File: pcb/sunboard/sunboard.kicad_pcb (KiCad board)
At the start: 2 copper layers, 3 parts, among them U1 CD74HC4067M, U2 CD74HC4067M, U3 ESP32_NODEMCU

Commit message: feat(pcb): remove led driver, layout main grid
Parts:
- added D1: WS2812B, LED_SMD:LED_WS2812B_PLCC4_5.0x5.0mm_P3.2mm, F.Cu at (20.0, 17.5)
- added D10: WS2812B, LED_SMD:LED_WS2812B_PLCC4_5.0x5.0mm_P3.2mm, F.Cu at (110.0, 17.5)
- added D100: WS2812B, LED_SMD:LED_WS2812B_PLCC4_5.0x5.0mm_P3.2mm, F.Cu at (20.0, 152.5)
- added D101: WS2812B, LED_SMD:LED_WS2812B_PLCC4_5.0x5.0mm_P3.2mm, F.Cu at (30.0, 152.5)
- added D102: WS2812B, LED_SMD:LED_WS2812B_PLCC4_5.0x5.0mm_P3.2mm, F.Cu at (40.0, 152.5)
- added D103: WS2812B, LED_SMD:LED_WS2812B_PLCC4_5.0x5.0mm_P3.2mm, F.Cu at (50.0, 152.5)
- added D104: WS2812B, LED_SMD:LED_WS2812B_PLCC4_5.0x5.0mm_P3.2mm, F.Cu at (60.0, 152.5)
- added D105: WS2812B, LED_SMD:LED_WS2812B_PLCC4_5.0x5.0mm_P3.2mm, F.Cu at (70.0, 152.5)
- added D106: WS2812B, LED_SMD:LED_WS2812B_PLCC4_5.0x5.0mm_P3.2mm, F.Cu at (80.0, 152.5)
- added D107: WS2812B, LED_SMD:LED_WS2812B_PLCC4_5.0x5.0mm_P3.2mm, F.Cu at (90.0, 152.5)
- added D108: WS2812B, LED_SMD:LED_WS2812B_PLCC4_5.0x5.0mm_P3.2mm, F.Cu at (100.0, 152.5)
- added D109: WS2812B, LED_SMD:LED_WS2812B_PLCC4_5.0x5.0mm_P3.2mm, F.Cu at (110.0, 152.5)
- added D11: WS2812B, LED_SMD:LED_WS2812B_PLCC4_5.0x5.0mm_P3.2mm, F.Cu at (120.0, 17.5)
- added D110: WS2812B, LED_SMD:LED_WS2812B_PLCC4_5.0x5.0mm_P3.2mm, F.Cu at (120.0, 152.5)
- added D111: WS2812B, LED_SMD:LED_WS2812B_PLCC4_5.0x5.0mm_P3.2mm, F.Cu at (20.0, 167.5)
- added D112: WS2812B, LED_SMD:LED_WS2812B_PLCC4_5.0x5.0mm_P3.2mm, F.Cu at (30.0, 167.5)
- added D113: WS2812B, LED_SMD:LED_WS2812B_PLCC4_5.0x5.0mm_P3.2mm, F.Cu at (40.0, 167.5)
- added D114: WS2812B, LED_SMD:LED_WS2812B_PLCC4_5.0x5.0mm_P3.2mm, F.Cu at (50.0, 167.5)
- added D115: WS2812B, LED_SMD:LED_WS2812B_PLCC4_5.0x5.0mm_P3.2mm, F.Cu at (60.0, 167.5)
- added D116: WS2812B, LED_SMD:LED_WS2812B_PLCC4_5.0x5.0mm_P3.2mm, F.Cu at (70.0, 167.5)
- added D117: WS2812B, LED_SMD:LED_WS2812B_PLCC4_5.0x5.0mm_P3.2mm, F.Cu at (80.0, 167.5)
- added D118: WS2812B, LED_SMD:LED_WS2812B_PLCC4_5.0x5.0mm_P3.2mm, F.Cu at (90.0, 167.5)
- added D119: WS2812B, LED_SMD:LED_WS2812B_PLCC4_5.0x5.0mm_P3.2mm, F.Cu at (100.0, 167.5)
- added D12: WS2812B, LED_SMD:LED_WS2812B_PLCC4_5.0x5.0mm_P3.2mm, F.Cu at (20.0, 32.5)
- added D120: WS2812B, LED_SMD:LED_WS2812B_PLCC4_5.0x5.0mm_P3.2mm, F.Cu at (110.0, 167.5)
- added D121: WS2812B, LED_SMD:LED_WS2812B_PLCC4_5.0x5.0mm_P3.2mm, F.Cu at (120.0, 167.5)
- added D122: WS2812B, LED_SMD:LED_WS2812B_PLCC4_5.0x5.0mm_P3.2mm, F.Cu at (20.0, 182.5)
- added D123: WS2812B, LED_SMD:LED_WS2812B_PLCC4_5.0x5.0mm_P3.2mm, F.Cu at (30.0, 182.5)
- added D124: WS2812B, LED_SMD:LED_WS2812B_PLCC4_5.0x5.0mm_P3.2mm, F.Cu at (40.0, 182.5)
- added D125: WS2812B, LED_SMD:LED_WS2812B_PLCC4_5.0x5.0mm_P3.2mm, F.Cu at (50.0, 182.5)
- added D126: WS2812B, LED_SMD:LED_WS2812B_PLCC4_5.0x5.0mm_P3.2mm, F.Cu at (60.0, 182.5)
- added D127: WS2812B, LED_SMD:LED_WS2812B_PLCC4_5.0x5.0mm_P3.2mm, F.Cu at (70.0, 182.5)
- added D128: WS2812B, LED_SMD:LED_WS2812B_PLCC4_5.0x5.0mm_P3.2mm, F.Cu at (80.0, 182.5)
- added D129: WS2812B, LED_SMD:LED_WS2812B_PLCC4_5.0x5.0mm_P3.2mm, F.Cu at (90.0, 182.5)
- added D13: WS2812B, LED_SMD:LED_WS2812B_PLCC4_5.0x5.0mm_P3.2mm, F.Cu at (30.0, 32.5)
- added D130: WS2812B, LED_SMD:LED_WS2812B_PLCC4_5.0x5.0mm_P3.2mm, F.Cu at (100.0, 182.5)
- added D131: WS2812B, LED_SMD:LED_WS2812B_PLCC4_5.0x5.0mm_P3.2mm, F.Cu at (110.0, 182.5)
- added D132: WS2812B, LED_SMD:LED_WS2812B_PLCC4_5.0x5.0mm_P3.2mm, F.Cu at (120.0, 182.5)
- added D133: WS2812B, LED_SMD:LED_WS2812B_PLCC4_5.0x5.0mm_P3.2mm, F.Cu at (20.0, 197.5)
- added D134: WS2812B, LED_SMD:LED_WS2812B_PLCC4_5.0x5.0mm_P3.2mm, F.Cu at (30.0, 197.5)
- added D135: WS2812B, LED_SMD:LED_WS2812B_PLCC4_5.0x5.0mm_P3.2mm, F.Cu at (40.0, 197.5)
- added D136: WS2812B, LED_SMD:LED_WS2812B_PLCC4_5.0x5.0mm_P3.2mm, F.Cu at (50.0, 197.5)
- added D137: WS2812B, LED_SMD:LED_WS2812B_PLCC4_5.0x5.0mm_P3.2mm, F.Cu at (60.0, 197.5)
- added D138: WS2812B, LED_SMD:LED_WS2812B_PLCC4_5.0x5.0mm_P3.2mm, F.Cu at (70.0, 197.5)
- added D139: WS2812B, LED_SMD:LED_WS2812B_PLCC4_5.0x5.0mm_P3.2mm, F.Cu at (80.0, 197.5)
- added D14: WS2812B, LED_SMD:LED_WS2812B_PLCC4_5.0x5.0mm_P3.2mm, F.Cu at (40.0, 32.5)
- added D140: WS2812B, LED_SMD:LED_WS2812B_PLCC4_5.0x5.0mm_P3.2mm, F.Cu at (90.0, 197.5)
- added D141: WS2812B, LED_SMD:LED_WS2812B_PLCC4_5.0x5.0mm_P3.2mm, F.Cu at (100.0, 197.5)
- added D142: WS2812B, LED_SMD:LED_WS2812B_PLCC4_5.0x5.0mm_P3.2mm, F.Cu at (110.0, 197.5)
- added D143: WS2812B, LED_SMD:LED_WS2812B_PLCC4_5.0x5.0mm_P3.2mm, F.Cu at (120.0, 197.5)
- added D144: WS2812B, LED_SMD:LED_WS2812B_PLCC4_5.0x5.0mm_P3.2mm, F.Cu at (20.0, 212.5)
- added D145: WS2812B, LED_SMD:LED_WS2812B_PLCC4_5.0x5.0mm_P3.2mm, F.Cu at (30.0, 212.5)
- added D146: WS2812B, LED_SMD:LED_WS2812B_PLCC4_5.0x5.0mm_P3.2mm, F.Cu at (40.0, 212.5)
- added D147: WS2812B, LED_SMD:LED_WS2812B_PLCC4_5.0x5.0mm_P3.2mm, F.Cu at (50.0, 212.5)
- added D148: WS2812B, LED_SMD:LED_WS2812B_PLCC4_5.0x5.0mm_P3.2mm, F.Cu at (60.0, 212.5)
- added D149: WS2812B, LED_SMD:LED_WS2812B_PLCC4_5.0x5.0mm_P3.2mm, F.Cu at (70.0, 212.5)
- added D15: WS2812B, LED_SMD:LED_WS2812B_PLCC4_5.0x5.0mm_P3.2mm, F.Cu at (50.0, 32.5)
- added D150: WS2812B, LED_SMD:LED_WS2812B_PLCC4_5.0x5.0mm_P3.2mm, F.Cu at (80.0, 212.5)
- added D151: WS2812B, LED_SMD:LED_WS2812B_PLCC4_5.0x5.0mm_P3.2mm, F.Cu at (90.0, 212.5)
- added D152: WS2812B, LED_SMD:LED_WS2812B_PLCC4_5.0x5.0mm_P3.2mm, F.Cu at (100.0, 212.5)
- added D153: WS2812B, LED_SMD:LED_WS2812B_PLCC4_5.0x5.0mm_P3.2mm, F.Cu at (110.0, 212.5)
- added D154: WS2812B, LED_SMD:LED_WS2812B_PLCC4_5.0x5.0mm_P3.2mm, F.Cu at (120.0, 212.5)
- added D16: WS2812B, LED_SMD:LED_WS2812B_PLCC4_5.0x5.0mm_P3.2mm, F.Cu at (60.0, 32.5)
- added D17: WS2812B, LED_SMD:LED_WS2812B_PLCC4_5.0x5.0mm_P3.2mm, F.Cu at (70.0, 32.5)
- added D18: WS2812B, LED_SMD:LED_WS2812B_PLCC4_5.0x5.0mm_P3.2mm, F.Cu at (80.0, 32.5)
- added D19: WS2812B, LED_SMD:LED_WS2812B_PLCC4_5.0x5.0mm_P3.2mm, F.Cu at (90.0, 32.5)
- added D2: WS2812B, LED_SMD:LED_WS2812B_PLCC4_5.0x5.0mm_P3.2mm, F.Cu at (30.0, 17.5)
- added D20: WS2812B, LED_SMD:LED_WS2812B_PLCC4_5.0x5.0mm_P3.2mm, F.Cu at (100.0, 32.5)
- added D21: WS2812B, LED_SMD:LED_WS2812B_PLCC4_5.0x5.0mm_P3.2mm, F.Cu at (110.0, 32.5)
- added D22: WS2812B, LED_SMD:LED_WS2812B_PLCC4_5.0x5.0mm_P3.2mm, F.Cu at (120.0, 32.5)
- added D23: WS2812B, LED_SMD:LED_WS2812B_PLCC4_5.0x5.0mm_P3.2mm, F.Cu at (20.0, 47.5)
- added D24: WS2812B, LED_SMD:LED_WS2812B_PLCC4_5.0x5.0mm_P3.2mm, F.Cu at (30.0, 47.5)
- added D25: WS2812B, LED_SMD:LED_WS2812B_PLCC4_5.0x5.0mm_P3.2mm, F.Cu at (40.0, 47.5)
- added D26: WS2812B, LED_SMD:LED_WS2812B_PLCC4_5.0x5.0mm_P3.2mm, F.Cu at (50.0, 47.5)
- added D27: WS2812B, LED_SMD:LED_WS2812B_PLCC4_5.0x5.0mm_P3.2mm, F.Cu at (60.0, 47.5)
- added D28: WS2812B, LED_SMD:LED_WS2812B_PLCC4_5.0x5.0mm_P3.2mm, F.Cu at (70.0, 47.5)
- added D29: WS2812B, LED_SMD:LED_WS2812B_PLCC4_5.0x5.0mm_P3.2mm, F.Cu at (80.0, 47.5)
- added D3: WS2812B, LED_SMD:LED_WS2812B_PLCC4_5.0x5.0mm_P3.2mm, F.Cu at (40.0, 17.5)
- added D30: WS2812B, LED_SMD:LED_WS2812B_PLCC4_5.0x5.0mm_P3.2mm, F.Cu at (90.0, 47.5)
- added D31: WS2812B, LED_SMD:LED_WS2812B_PLCC4_5.0x5.0mm_P3.2mm, F.Cu at (100.0, 47.5)
- added D32: WS2812B, LED_SMD:LED_WS2812B_PLCC4_5.0x5.0mm_P3.2mm, F.Cu at (110.0, 47.5)
- added D33: WS2812B, LED_SMD:LED_WS2812B_PLCC4_5.0x5.0mm_P3.2mm, F.Cu at (120.0, 47.5)
- added D34: WS2812B, LED_SMD:LED_WS2812B_PLCC4_5.0x5.0mm_P3.2mm, F.Cu at (20.0, 62.5)
- added D35: WS2812B, LED_SMD:LED_WS2812B_PLCC4_5.0x5.0mm_P3.2mm, F.Cu at (30.0, 62.5)
- added D36: WS2812B, LED_SMD:LED_WS2812B_PLCC4_5.0x5.0mm_P3.2mm, F.Cu at (40.0, 62.5)
- added D37: WS2812B, LED_SMD:LED_WS2812B_PLCC4_5.0x5.0mm_P3.2mm, F.Cu at (50.0, 62.5)
- added D38: WS2812B, LED_SMD:LED_WS2812B_PLCC4_5.0x5.0mm_P3.2mm, F.Cu at (60.0, 62.5)
- added D39: WS2812B, LED_SMD:LED_WS2812B_PLCC4_5.0x5.0mm_P3.2mm, F.Cu at (70.0, 62.5)
- added D4: WS2812B, LED_SMD:LED_WS2812B_PLCC4_5.0x5.0mm_P3.2mm, F.Cu at (50.0, 17.5)
- added D40: WS2812B, LED_SMD:LED_WS2812B_PLCC4_5.0x5.0mm_P3.2mm, F.Cu at (80.0, 62.5)
- added D41: WS2812B, LED_SMD:LED_WS2812B_PLCC4_5.0x5.0mm_P3.2mm, F.Cu at (90.0, 62.5)
- added D42: WS2812B, LED_SMD:LED_WS2812B_PLCC4_5.0x5.0mm_P3.2mm, F.Cu at (100.0, 62.5)
- added D43: WS2812B, LED_SMD:LED_WS2812B_PLCC4_5.0x5.0mm_P3.2mm, F.Cu at (110.0, 62.5)
- added D44: WS2812B, LED_SMD:LED_WS2812B_PLCC4_5.0x5.0mm_P3.2mm, F.Cu at (120.0, 62.5)
- added D45: WS2812B, LED_SMD:LED_WS2812B_PLCC4_5.0x5.0mm_P3.2mm, F.Cu at (20.0, 77.5)
- added D46: WS2812B, LED_SMD:LED_WS2812B_PLCC4_5.0x5.0mm_P3.2mm, F.Cu at (30.0, 77.5)
- added D47: WS2812B, LED_SMD:LED_WS2812B_PLCC4_5.0x5.0mm_P3.2mm, F.Cu at (40.0, 77.5)
- added D48: WS2812B, LED_SMD:LED_WS2812B_PLCC4_5.0x5.0mm_P3.2mm, F.Cu at (50.0, 77.5)
- added D49: WS2812B, LED_SMD:LED_WS2812B_PLCC4_5.0x5.0mm_P3.2mm, F.Cu at (60.0, 77.5)
- added D5: WS2812B, LED_SMD:LED_WS2812B_PLCC4_5.0x5.0mm_P3.2mm, F.Cu at (60.0, 17.5)
- added D50: WS2812B, LED_SMD:LED_WS2812B_PLCC4_5.0x5.0mm_P3.2mm, F.Cu at (70.0, 77.5)
- added D51: WS2812B, LED_SMD:LED_WS2812B_PLCC4_5.0x5.0mm_P3.2mm, F.Cu at (80.0, 77.5)
- added D52: WS2812B, LED_SMD:LED_WS2812B_PLCC4_5.0x5.0mm_P3.2mm, F.Cu at (90.0, 77.5)
- added D53: WS2812B, LED_SMD:LED_WS2812B_PLCC4_5.0x5.0mm_P3.2mm, F.Cu at (100.0, 77.5)
- added D54: WS2812B, LED_SMD:LED_WS2812B_PLCC4_5.0x5.0mm_P3.2mm, F.Cu at (110.0, 77.5)
- added D55: WS2812B, LED_SMD:LED_WS2812B_PLCC4_5.0x5.0mm_P3.2mm, F.Cu at (120.0, 77.5)
- added D56: WS2812B, LED_SMD:LED_WS2812B_PLCC4_5.0x5.0mm_P3.2mm, F.Cu at (20.0, 92.5)
- added D57: WS2812B, LED_SMD:LED_WS2812B_PLCC4_5.0x5.0mm_P3.2mm, F.Cu at (30.0, 92.5)
- added D58: WS2812B, LED_SMD:LED_WS2812B_PLCC4_5.0x5.0mm_P3.2mm, F.Cu at (40.0, 92.5)
- added D59: WS2812B, LED_SMD:LED_WS2812B_PLCC4_5.0x5.0mm_P3.2mm, F.Cu at (50.0, 92.5)
- added D6: WS2812B, LED_SMD:LED_WS2812B_PLCC4_5.0x5.0mm_P3.2mm, F.Cu at (70.0, 17.5)
- added D60: WS2812B, LED_SMD:LED_WS2812B_PLCC4_5.0x5.0mm_P3.2mm, F.Cu at (60.0, 92.5)
- added D61: WS2812B, LED_SMD:LED_WS2812B_PLCC4_5.0x5.0mm_P3.2mm, F.Cu at (70.0, 92.5)
- added D62: WS2812B, LED_SMD:LED_WS2812B_PLCC4_5.0x5.0mm_P3.2mm, F.Cu at (80.0, 92.5)
- added D63: WS2812B, LED_SMD:LED_WS2812B_PLCC4_5.0x5.0mm_P3.2mm, F.Cu at (90.0, 92.5)
- added D64: WS2812B, LED_SMD:LED_WS2812B_PLCC4_5.0x5.0mm_P3.2mm, F.Cu at (100.0, 92.5)
- added D65: WS2812B, LED_SMD:LED_WS2812B_PLCC4_5.0x5.0mm_P3.2mm, F.Cu at (110.0, 92.5)
- added D66: WS2812B, LED_SMD:LED_WS2812B_PLCC4_5.0x5.0mm_P3.2mm, F.Cu at (120.0, 92.5)
- added D67: WS2812B, LED_SMD:LED_WS2812B_PLCC4_5.0x5.0mm_P3.2mm, F.Cu at (20.0, 107.5)
- added D68: WS2812B, LED_SMD:LED_WS2812B_PLCC4_5.0x5.0mm_P3.2mm, F.Cu at (30.0, 107.5)
- added D69: WS2812B, LED_SMD:LED_WS2812B_PLCC4_5.0x5.0mm_P3.2mm, F.Cu at (40.0, 107.5)
- added D7: WS2812B, LED_SMD:LED_WS2812B_PLCC4_5.0x5.0mm_P3.2mm, F.Cu at (80.0, 17.5)
- added D70: WS2812B, LED_SMD:LED_WS2812B_PLCC4_5.0x5.0mm_P3.2mm, F.Cu at (50.0, 107.5)
- added D71: WS2812B, LED_SMD:LED_WS2812B_PLCC4_5.0x5.0mm_P3.2mm, F.Cu at (60.0, 107.5)
- added D72: WS2812B, LED_SMD:LED_WS2812B_PLCC4_5.0x5.0mm_P3.2mm, F.Cu at (70.0, 107.5)
- added D73: WS2812B, LED_SMD:LED_WS2812B_PLCC4_5.0x5.0mm_P3.2mm, F.Cu at (80.0, 107.5)
- added D74: WS2812B, LED_SMD:LED_WS2812B_PLCC4_5.0x5.0mm_P3.2mm, F.Cu at (90.0, 107.5)
- added D75: WS2812B, LED_SMD:LED_WS2812B_PLCC4_5.0x5.0mm_P3.2mm, F.Cu at (100.0, 107.5)
- added D76: WS2812B, LED_SMD:LED_WS2812B_PLCC4_5.0x5.0mm_P3.2mm, F.Cu at (110.0, 107.5)
- added D77: WS2812B, LED_SMD:LED_WS2812B_PLCC4_5.0x5.0mm_P3.2mm, F.Cu at (120.0, 107.5)
- added D78: WS2812B, LED_SMD:LED_WS2812B_PLCC4_5.0x5.0mm_P3.2mm, F.Cu at (20.0, 122.5)
- added D79: WS2812B, LED_SMD:LED_WS2812B_PLCC4_5.0x5.0mm_P3.2mm, F.Cu at (30.0, 122.5)
- added D8: WS2812B, LED_SMD:LED_WS2812B_PLCC4_5.0x5.0mm_P3.2mm, F.Cu at (90.0, 17.5)
- added D80: WS2812B, LED_SMD:LED_WS2812B_PLCC4_5.0x5.0mm_P3.2mm, F.Cu at (40.0, 122.5)
- added D81: WS2812B, LED_SMD:LED_WS2812B_PLCC4_5.0x5.0mm_P3.2mm, F.Cu at (50.0, 122.5)
- added D82: WS2812B, LED_SMD:LED_WS2812B_PLCC4_5.0x5.0mm_P3.2mm, F.Cu at (60.0, 122.5)
- added D83: WS2812B, LED_SMD:LED_WS2812B_PLCC4_5.0x5.0mm_P3.2mm, F.Cu at (70.0, 122.5)
- added D84: WS2812B, LED_SMD:LED_WS2812B_PLCC4_5.0x5.0mm_P3.2mm, F.Cu at (80.0, 122.5)
- added D85: WS2812B, LED_SMD:LED_WS2812B_PLCC4_5.0x5.0mm_P3.2mm, F.Cu at (90.0, 122.5)
- added D86: WS2812B, LED_SMD:LED_WS2812B_PLCC4_5.0x5.0mm_P3.2mm, F.Cu at (100.0, 122.5)
- added D87: WS2812B, LED_SMD:LED_WS2812B_PLCC4_5.0x5.0mm_P3.2mm, F.Cu at (110.0, 122.5)
- added D88: WS2812B, LED_SMD:LED_WS2812B_PLCC4_5.0x5.0mm_P3.2mm, F.Cu at (120.0, 122.5)
- added D89: WS2812B, LED_SMD:LED_WS2812B_PLCC4_5.0x5.0mm_P3.2mm, F.Cu at (20.0, 137.5)
- added D9: WS2812B, LED_SMD:LED_WS2812B_PLCC4_5.0x5.0mm_P3.2mm, F.Cu at (100.0, 17.5)
- added D90: WS2812B, LED_SMD:LED_WS2812B_PLCC4_5.0x5.0mm_P3.2mm, F.Cu at (30.0, 137.5)
- added D91: WS2812B, LED_SMD:LED_WS2812B_PLCC4_5.0x5.0mm_P3.2mm, F.Cu at (40.0, 137.5)
- added D92: WS2812B, LED_SMD:LED_WS2812B_PLCC4_5.0x5.0mm_P3.2mm, F.Cu at (50.0, 137.5)
- added D93: WS2812B, LED_SMD:LED_WS2812B_PLCC4_5.0x5.0mm_P3.2mm, F.Cu at (60.0, 137.5)
- added D94: WS2812B, LED_SMD:LED_WS2812B_PLCC4_5.0x5.0mm_P3.2mm, F.Cu at (70.0, 137.5)
- added D95: WS2812B, LED_SMD:LED_WS2812B_PLCC4_5.0x5.0mm_P3.2mm, F.Cu at (80.0, 137.5)
- added D96: WS2812B, LED_SMD:LED_WS2812B_PLCC4_5.0x5.0mm_P3.2mm, F.Cu at (90.0, 137.5)
- added D97: WS2812B, LED_SMD:LED_WS2812B_PLCC4_5.0x5.0mm_P3.2mm, F.Cu at (100.0, 137.5)
- added D98: WS2812B, LED_SMD:LED_WS2812B_PLCC4_5.0x5.0mm_P3.2mm, F.Cu at (110.0, 137.5)
- added D99: WS2812B, LED_SMD:LED_WS2812B_PLCC4_5.0x5.0mm_P3.2mm, F.Cu at (120.0, 137.5)
- added SW1: SW_Push, Button_Switch_SMD:SW_Tactile_SPST_NO_Straight_CK_PTS636Sx25SMTRLFS, F.Cu at (20.0, 25.0)
- added SW10: SW_Push, Button_Switch_SMD:SW_Tactile_SPST_NO_Straight_CK_PTS636Sx25SMTRLFS, F.Cu at (110.0, 25.0)
- added SW100: SW_Push, Button_Switch_SMD:SW_Tactile_SPST_NO_Straight_CK_PTS636Sx25SMTRLFS, F.Cu at (20.0, 160.0)
- added SW101: SW_Push, Button_Switch_SMD:SW_Tactile_SPST_NO_Straight_CK_PTS636Sx25SMTRLFS, F.Cu at (30.0, 160.0)
- added SW102: SW_Push, Button_Switch_SMD:SW_Tactile_SPST_NO_Straight_CK_PTS636Sx25SMTRLFS, F.Cu at (40.0, 160.0)
- added SW103: SW_Push, Button_Switch_SMD:SW_Tactile_SPST_NO_Straight_CK_PTS636Sx25SMTRLFS, F.Cu at (50.0, 160.0)
- added SW104: SW_Push, Button_Switch_SMD:SW_Tactile_SPST_NO_Straight_CK_PTS636Sx25SMTRLFS, F.Cu at (60.0, 160.0)
- added SW105: SW_Push, Button_Switch_SMD:SW_Tactile_SPST_NO_Straight_CK_PTS636Sx25SMTRLFS, F.Cu at (70.0, 160.0)
- added SW106: SW_Push, Button_Switch_SMD:SW_Tactile_SPST_NO_Straight_CK_PTS636Sx25SMTRLFS, F.Cu at (80.0, 160.0)
- added SW107: SW_Push, Button_Switch_SMD:SW_Tactile_SPST_NO_Straight_CK_PTS636Sx25SMTRLFS, F.Cu at (90.0, 160.0)
- added SW108: SW_Push, Button_Switch_SMD:SW_Tactile_SPST_NO_Straight_CK_PTS636Sx25SMTRLFS, F.Cu at (100.0, 160.0)
- added SW109: SW_Push, Button_Switch_SMD:SW_Tactile_SPST_NO_Straight_CK_PTS636Sx25SMTRLFS, F.Cu at (110.0, 160.0)
- added SW11: SW_Push, Button_Switch_SMD:SW_Tactile_SPST_NO_Straight_CK_PTS636Sx25SMTRLFS, F.Cu at (120.0, 25.0)
- added SW110: SW_Push, Button_Switch_SMD:SW_Tactile_SPST_NO_Straight_CK_PTS636Sx25SMTRLFS, F.Cu at (120.0, 160.0)
- added SW111: SW_Push, Button_Switch_SMD:SW_Tactile_SPST_NO_Straight_CK_PTS636Sx25SMTRLFS, F.Cu at (20.0, 175.0)
- added SW112: SW_Push, Button_Switch_SMD:SW_Tactile_SPST_NO_Straight_CK_PTS636Sx25SMTRLFS, F.Cu at (30.0, 175.0)
- added SW113: SW_Push, Button_Switch_SMD:SW_Tactile_SPST_NO_Straight_CK_PTS636Sx25SMTRLFS, F.Cu at (40.0, 175.0)
- added SW114: SW_Push, Button_Switch_SMD:SW_Tactile_SPST_NO_Straight_CK_PTS636Sx25SMTRLFS, F.Cu at (50.0, 175.0)
- added SW115: SW_Push, Button_Switch_SMD:SW_Tactile_SPST_NO_Straight_CK_PTS636Sx25SMTRLFS, F.Cu at (60.0, 175.0)
- added SW116: SW_Push, Button_Switch_SMD:SW_Tactile_SPST_NO_Straight_CK_PTS636Sx25SMTRLFS, F.Cu at (70.0, 175.0)
- added SW117: SW_Push, Button_Switch_SMD:SW_Tactile_SPST_NO_Straight_CK_PTS636Sx25SMTRLFS, F.Cu at (80.0, 175.0)
- added SW118: SW_Push, Button_Switch_SMD:SW_Tactile_SPST_NO_Straight_CK_PTS636Sx25SMTRLFS, F.Cu at (90.0, 175.0)
- added SW119: SW_Push, Button_Switch_SMD:SW_Tactile_SPST_NO_Straight_CK_PTS636Sx25SMTRLFS, F.Cu at (100.0, 175.0)
- added SW12: SW_Push, Button_Switch_SMD:SW_Tactile_SPST_NO_Straight_CK_PTS636Sx25SMTRLFS, F.Cu at (20.0, 40.0)
- added SW120: SW_Push, Button_Switch_SMD:SW_Tactile_SPST_NO_Straight_CK_PTS636Sx25SMTRLFS, F.Cu at (110.0, 175.0)
- added SW121: SW_Push, Button_Switch_SMD:SW_Tactile_SPST_NO_Straight_CK_PTS636Sx25SMTRLFS, F.Cu at (120.0, 175.0)
- added SW122: SW_Push, Button_Switch_SMD:SW_Tactile_SPST_NO_Straight_CK_PTS636Sx25SMTRLFS, F.Cu at (20.0, 190.0)
- added SW123: SW_Push, Button_Switch_SMD:SW_Tactile_SPST_NO_Straight_CK_PTS636Sx25SMTRLFS, F.Cu at (30.0, 190.0)
- added SW124: SW_Push, Button_Switch_SMD:SW_Tactile_SPST_NO_Straight_CK_PTS636Sx25SMTRLFS, F.Cu at (40.0, 190.0)
- added SW125: SW_Push, Button_Switch_SMD:SW_Tactile_SPST_NO_Straight_CK_PTS636Sx25SMTRLFS, F.Cu at (50.0, 190.0)
- added SW126: SW_Push, Button_Switch_SMD:SW_Tactile_SPST_NO_Straight_CK_PTS636Sx25SMTRLFS, F.Cu at (60.0, 190.0)
- added SW127: SW_Push, Button_Switch_SMD:SW_Tactile_SPST_NO_Straight_CK_PTS636Sx25SMTRLFS, F.Cu at (70.0, 190.0)
- added SW128: SW_Push, Button_Switch_SMD:SW_Tactile_SPST_NO_Straight_CK_PTS636Sx25SMTRLFS, F.Cu at (80.0, 190.0)
- added SW129: SW_Push, Button_Switch_SMD:SW_Tactile_SPST_NO_Straight_CK_PTS636Sx25SMTRLFS, F.Cu at (90.0, 190.0)
- added SW13: SW_Push, Button_Switch_SMD:SW_Tactile_SPST_NO_Straight_CK_PTS636Sx25SMTRLFS, F.Cu at (30.0, 40.0)
- added SW130: SW_Push, Button_Switch_SMD:SW_Tactile_SPST_NO_Straight_CK_PTS636Sx25SMTRLFS, F.Cu at (100.0, 190.0)
- added SW131: SW_Push, Button_Switch_SMD:SW_Tactile_SPST_NO_Straight_CK_PTS636Sx25SMTRLFS, F.Cu at (110.0, 190.0)
- added SW132: SW_Push, Button_Switch_SMD:SW_Tactile_SPST_NO_Straight_CK_PTS636Sx25SMTRLFS, F.Cu at (120.0, 190.0)
- added SW133: SW_Push, Button_Switch_SMD:SW_Tactile_SPST_NO_Straight_CK_PTS636Sx25SMTRLFS, F.Cu at (20.0, 205.0)
- added SW134: SW_Push, Button_Switch_SMD:SW_Tactile_SPST_NO_Straight_CK_PTS636Sx25SMTRLFS, F.Cu at (30.0, 205.0)
- added SW135: SW_Push, Button_Switch_SMD:SW_Tactile_SPST_NO_Straight_CK_PTS636Sx25SMTRLFS, F.Cu at (40.0, 205.0)
- added SW136: SW_Push, Button_Switch_SMD:SW_Tactile_SPST_NO_Straight_CK_PTS636Sx25SMTRLFS, F.Cu at (50.0, 205.0)
- added SW137: SW_Push, Button_Switch_SMD:SW_Tactile_SPST_NO_Straight_CK_PTS636Sx25SMTRLFS, F.Cu at (60.0, 205.0)
- added SW138: SW_Push, Button_Switch_SMD:SW_Tactile_SPST_NO_Straight_CK_PTS636Sx25SMTRLFS, F.Cu at (70.0, 205.0)
- added SW139: SW_Push, Button_Switch_SMD:SW_Tactile_SPST_NO_Straight_CK_PTS636Sx25SMTRLFS, F.Cu at (80.0, 205.0)
- added SW14: SW_Push, Button_Switch_SMD:SW_Tactile_SPST_NO_Straight_CK_PTS636Sx25SMTRLFS, F.Cu at (40.0, 40.0)
- added SW140: SW_Push, Button_Switch_SMD:SW_Tactile_SPST_NO_Straight_CK_PTS636Sx25SMTRLFS, F.Cu at (90.0, 205.0)
- added SW141: SW_Push, Button_Switch_SMD:SW_Tactile_SPST_NO_Straight_CK_PTS636Sx25SMTRLFS, F.Cu at (100.0, 205.0)
- added SW142: SW_Push, Button_Switch_SMD:SW_Tactile_SPST_NO_Straight_CK_PTS636Sx25SMTRLFS, F.Cu at (110.0, 205.0)
- added SW143: SW_Push, Button_Switch_SMD:SW_Tactile_SPST_NO_Straight_CK_PTS636Sx25SMTRLFS, F.Cu at (120.0, 205.0)
- added SW144: SW_Push, Button_Switch_SMD:SW_Tactile_SPST_NO_Straight_CK_PTS636Sx25SMTRLFS, F.Cu at (20.0, 220.0)
- added SW145: SW_Push, Button_Switch_SMD:SW_Tactile_SPST_NO_Straight_CK_PTS636Sx25SMTRLFS, F.Cu at (30.0, 220.0)
- added SW146: SW_Push, Button_Switch_SMD:SW_Tactile_SPST_NO_Straight_CK_PTS636Sx25SMTRLFS, F.Cu at (40.0, 220.0)
- added SW147: SW_Push, Button_Switch_SMD:SW_Tactile_SPST_NO_Straight_CK_PTS636Sx25SMTRLFS, F.Cu at (50.0, 220.0)
- added SW148: SW_Push, Button_Switch_SMD:SW_Tactile_SPST_NO_Straight_CK_PTS636Sx25SMTRLFS, F.Cu at (60.0, 220.0)
- added SW149: SW_Push, Button_Switch_SMD:SW_Tactile_SPST_NO_Straight_CK_PTS636Sx25SMTRLFS, F.Cu at (70.0, 220.0)
- added SW15: SW_Push, Button_Switch_SMD:SW_Tactile_SPST_NO_Straight_CK_PTS636Sx25SMTRLFS, F.Cu at (50.0, 40.0)
- added SW150: SW_Push, Button_Switch_SMD:SW_Tactile_SPST_NO_Straight_CK_PTS636Sx25SMTRLFS, F.Cu at (80.0, 220.0)
- added SW151: SW_Push, Button_Switch_SMD:SW_Tactile_SPST_NO_Straight_CK_PTS636Sx25SMTRLFS, F.Cu at (90.0, 220.0)
- added SW152: SW_Push, Button_Switch_SMD:SW_Tactile_SPST_NO_Straight_CK_PTS636Sx25SMTRLFS, F.Cu at (100.0, 220.0)
- added SW153: SW_Push, Button_Switch_SMD:SW_Tactile_SPST_NO_Straight_CK_PTS636Sx25SMTRLFS, F.Cu at (110.0, 220.0)
- added SW154: SW_Push, Button_Switch_SMD:SW_Tactile_SPST_NO_Straight_CK_PTS636Sx25SMTRLFS, F.Cu at (120.0, 220.0)
- added SW16: SW_Push, Button_Switch_SMD:SW_Tactile_SPST_NO_Straight_CK_PTS636Sx25SMTRLFS, F.Cu at (60.0, 40.0)
- added SW17: SW_Push, Button_Switch_SMD:SW_Tactile_SPST_NO_Straight_CK_PTS636Sx25SMTRLFS, F.Cu at (70.0, 40.0)
- added SW18: SW_Push, Button_Switch_SMD:SW_Tactile_SPST_NO_Straight_CK_PTS636Sx25SMTRLFS, F.Cu at (80.0, 40.0)
- added SW19: SW_Push, Button_Switch_SMD:SW_Tactile_SPST_NO_Straight_CK_PTS636Sx25SMTRLFS, F.Cu at (90.0, 40.0)
- added SW2: SW_Push, Button_Switch_SMD:SW_Tactile_SPST_NO_Straight_CK_PTS636Sx25SMTRLFS, F.Cu at (30.0, 25.0)
- added SW20: SW_Push, Button_Switch_SMD:SW_Tactile_SPST_NO_Straight_CK_PTS636Sx25SMTRLFS, F.Cu at (100.0, 40.0)
- added SW21: SW_Push, Button_Switch_SMD:SW_Tactile_SPST_NO_Straight_CK_PTS636Sx25SMTRLFS, F.Cu at (110.0, 40.0)
- added SW22: SW_Push, Button_Switch_SMD:SW_Tactile_SPST_NO_Straight_CK_PTS636Sx25SMTRLFS, F.Cu at (120.0, 40.0)
- added SW23: SW_Push, Button_Switch_SMD:SW_Tactile_SPST_NO_Straight_CK_PTS636Sx25SMTRLFS, F.Cu at (20.0, 55.0)
- added SW24: SW_Push, Button_Switch_SMD:SW_Tactile_SPST_NO_Straight_CK_PTS636Sx25SMTRLFS, F.Cu at (30.0, 55.0)
- added SW25: SW_Push, Button_Switch_SMD:SW_Tactile_SPST_NO_Straight_CK_PTS636Sx25SMTRLFS, F.Cu at (40.0, 55.0)
- added SW26: SW_Push, Button_Switch_SMD:SW_Tactile_SPST_NO_Straight_CK_PTS636Sx25SMTRLFS, F.Cu at (50.0, 55.0)
- added SW27: SW_Push, Button_Switch_SMD:SW_Tactile_SPST_NO_Straight_CK_PTS636Sx25SMTRLFS, F.Cu at (60.0, 55.0)
- added SW28: SW_Push, Button_Switch_SMD:SW_Tactile_SPST_NO_Straight_CK_PTS636Sx25SMTRLFS, F.Cu at (70.0, 55.0)
- added SW29: SW_Push, Button_Switch_SMD:SW_Tactile_SPST_NO_Straight_CK_PTS636Sx25SMTRLFS, F.Cu at (80.0, 55.0)
- added SW3: SW_Push, Button_Switch_SMD:SW_Tactile_SPST_NO_Straight_CK_PTS636Sx25SMTRLFS, F.Cu at (40.0, 25.0)
- added SW30: SW_Push, Button_Switch_SMD:SW_Tactile_SPST_NO_Straight_CK_PTS636Sx25SMTRLFS, F.Cu at (90.0, 55.0)
- added SW31: SW_Push, Button_Switch_SMD:SW_Tactile_SPST_NO_Straight_CK_PTS636Sx25SMTRLFS, F.Cu at (100.0, 55.0)
- added SW32: SW_Push, Button_Switch_SMD:SW_Tactile_SPST_NO_Straight_CK_PTS636Sx25SMTRLFS, F.Cu at (110.0, 55.0)
- added SW33: SW_Push, Button_Switch_SMD:SW_Tactile_SPST_NO_Straight_CK_PTS636Sx25SMTRLFS, F.Cu at (120.0, 55.0)
- added SW34: SW_Push, Button_Switch_SMD:SW_Tactile_SPST_NO_Straight_CK_PTS636Sx25SMTRLFS, F.Cu at (20.0, 70.0)
- added SW35: SW_Push, Button_Switch_SMD:SW_Tactile_SPST_NO_Straight_CK_PTS636Sx25SMTRLFS, F.Cu at (30.0, 70.0)
- added SW36: SW_Push, Button_Switch_SMD:SW_Tactile_SPST_NO_Straight_CK_PTS636Sx25SMTRLFS, F.Cu at (40.0, 70.0)
- added SW37: SW_Push, Button_Switch_SMD:SW_Tactile_SPST_NO_Straight_CK_PTS636Sx25SMTRLFS, F.Cu at (50.0, 70.0)
- added SW38: SW_Push, Button_Switch_SMD:SW_Tactile_SPST_NO_Straight_CK_PTS636Sx25SMTRLFS, F.Cu at (60.0, 70.0)
- added SW39: SW_Push, Button_Switch_SMD:SW_Tactile_SPST_NO_Straight_CK_PTS636Sx25SMTRLFS, F.Cu at (70.0, 70.0)
- added SW4: SW_Push, Button_Switch_SMD:SW_Tactile_SPST_NO_Straight_CK_PTS636Sx25SMTRLFS, F.Cu at (50.0, 25.0)
- added SW40: SW_Push, Button_Switch_SMD:SW_Tactile_SPST_NO_Straight_CK_PTS636Sx25SMTRLFS, F.Cu at (80.0, 70.0)
- added SW41: SW_Push, Button_Switch_SMD:SW_Tactile_SPST_NO_Straight_CK_PTS636Sx25SMTRLFS, F.Cu at (90.0, 70.0)
- added SW42: SW_Push, Button_Switch_SMD:SW_Tactile_SPST_NO_Straight_CK_PTS636Sx25SMTRLFS, F.Cu at (100.0, 70.0)
- added SW43: SW_Push, Button_Switch_SMD:SW_Tactile_SPST_NO_Straight_CK_PTS636Sx25SMTRLFS, F.Cu at (110.0, 70.0)
- added SW44: SW_Push, Button_Switch_SMD:SW_Tactile_SPST_NO_Straight_CK_PTS636Sx25SMTRLFS, F.Cu at (120.0, 70.0)
- added SW45: SW_Push, Button_Switch_SMD:SW_Tactile_SPST_NO_Straight_CK_PTS636Sx25SMTRLFS, F.Cu at (20.0, 85.0)
- added SW46: SW_Push, Button_Switch_SMD:SW_Tactile_SPST_NO_Straight_CK_PTS636Sx25SMTRLFS, F.Cu at (30.0, 85.0)
- added SW47: SW_Push, Button_Switch_SMD:SW_Tactile_SPST_NO_Straight_CK_PTS636Sx25SMTRLFS, F.Cu at (40.0, 85.0)
- added SW48: SW_Push, Button_Switch_SMD:SW_Tactile_SPST_NO_Straight_CK_PTS636Sx25SMTRLFS, F.Cu at (50.0, 85.0)
- added SW49: SW_Push, Button_Switch_SMD:SW_Tactile_SPST_NO_Straight_CK_PTS636Sx25SMTRLFS, F.Cu at (60.0, 85.0)
- added SW5: SW_Push, Button_Switch_SMD:SW_Tactile_SPST_NO_Straight_CK_PTS636Sx25SMTRLFS, F.Cu at (60.0, 25.0)
- added SW50: SW_Push, Button_Switch_SMD:SW_Tactile_SPST_NO_Straight_CK_PTS636Sx25SMTRLFS, F.Cu at (70.0, 85.0)
- added SW51: SW_Push, Button_Switch_SMD:SW_Tactile_SPST_NO_Straight_CK_PTS636Sx25SMTRLFS, F.Cu at (80.0, 85.0)
- added SW52: SW_Push, Button_Switch_SMD:SW_Tactile_SPST_NO_Straight_CK_PTS636Sx25SMTRLFS, F.Cu at (90.0, 85.0)
- added SW53: SW_Push, Button_Switch_SMD:SW_Tactile_SPST_NO_Straight_CK_PTS636Sx25SMTRLFS, F.Cu at (100.0, 85.0)
- added SW54: SW_Push, Button_Switch_SMD:SW_Tactile_SPST_NO_Straight_CK_PTS636Sx25SMTRLFS, F.Cu at (110.0, 85.0)
- added SW55: SW_Push, Button_Switch_SMD:SW_Tactile_SPST_NO_Straight_CK_PTS636Sx25SMTRLFS, F.Cu at (120.0, 85.0)
- added SW56: SW_Push, Button_Switch_SMD:SW_Tactile_SPST_NO_Straight_CK_PTS636Sx25SMTRLFS, F.Cu at (20.0, 100.0)
- added SW57: SW_Push, Button_Switch_SMD:SW_Tactile_SPST_NO_Straight_CK_PTS636Sx25SMTRLFS, F.Cu at (30.0, 100.0)
- added SW58: SW_Push, Button_Switch_SMD:SW_Tactile_SPST_NO_Straight_CK_PTS636Sx25SMTRLFS, F.Cu at (40.0, 100.0)
- added SW59: SW_Push, Button_Switch_SMD:SW_Tactile_SPST_NO_Straight_CK_PTS636Sx25SMTRLFS, F.Cu at (50.0, 100.0)
- added SW6: SW_Push, Button_Switch_SMD:SW_Tactile_SPST_NO_Straight_CK_PTS636Sx25SMTRLFS, F.Cu at (70.0, 25.0)
- added SW60: SW_Push, Button_Switch_SMD:SW_Tactile_SPST_NO_Straight_CK_PTS636Sx25SMTRLFS, F.Cu at (60.0, 100.0)
- added SW61: SW_Push, Button_Switch_SMD:SW_Tactile_SPST_NO_Straight_CK_PTS636Sx25SMTRLFS, F.Cu at (70.0, 100.0)
- added SW62: SW_Push, Button_Switch_SMD:SW_Tactile_SPST_NO_Straight_CK_PTS636Sx25SMTRLFS, F.Cu at (80.0, 100.0)
- added SW63: SW_Push, Button_Switch_SMD:SW_Tactile_SPST_NO_Straight_CK_PTS636Sx25SMTRLFS, F.Cu at (90.0, 100.0)
- added SW64: SW_Push, Button_Switch_SMD:SW_Tactile_SPST_NO_Straight_CK_PTS636Sx25SMTRLFS, F.Cu at (100.0, 100.0)
- added SW65: SW_Push, Button_Switch_SMD:SW_Tactile_SPST_NO_Straight_CK_PTS636Sx25SMTRLFS, F.Cu at (110.0, 100.0)
- added SW66: SW_Push, Button_Switch_SMD:SW_Tactile_SPST_NO_Straight_CK_PTS636Sx25SMTRLFS, F.Cu at (120.0, 100.0)
- added SW67: SW_Push, Button_Switch_SMD:SW_Tactile_SPST_NO_Straight_CK_PTS636Sx25SMTRLFS, F.Cu at (20.0, 115.0)
- added SW68: SW_Push, Button_Switch_SMD:SW_Tactile_SPST_NO_Straight_CK_PTS636Sx25SMTRLFS, F.Cu at (30.0, 115.0)
- added SW69: SW_Push, Button_Switch_SMD:SW_Tactile_SPST_NO_Straight_CK_PTS636Sx25SMTRLFS, F.Cu at (40.0, 115.0)
- added SW7: SW_Push, Button_Switch_SMD:SW_Tactile_SPST_NO_Straight_CK_PTS636Sx25SMTRLFS, F.Cu at (80.0, 25.0)
- added SW70: SW_Push, Button_Switch_SMD:SW_Tactile_SPST_NO_Straight_CK_PTS636Sx25SMTRLFS, F.Cu at (50.0, 115.0)
- added SW71: SW_Push, Button_Switch_SMD:SW_Tactile_SPST_NO_Straight_CK_PTS636Sx25SMTRLFS, F.Cu at (60.0, 115.0)
- added SW72: SW_Push, Button_Switch_SMD:SW_Tactile_SPST_NO_Straight_CK_PTS636Sx25SMTRLFS, F.Cu at (70.0, 115.0)
- added SW73: SW_Push, Button_Switch_SMD:SW_Tactile_SPST_NO_Straight_CK_PTS636Sx25SMTRLFS, F.Cu at (80.0, 115.0)
- added SW74: SW_Push, Button_Switch_SMD:SW_Tactile_SPST_NO_Straight_CK_PTS636Sx25SMTRLFS, F.Cu at (90.0, 115.0)
- added SW75: SW_Push, Button_Switch_SMD:SW_Tactile_SPST_NO_Straight_CK_PTS636Sx25SMTRLFS, F.Cu at (100.0, 115.0)
- added SW76: SW_Push, Button_Switch_SMD:SW_Tactile_SPST_NO_Straight_CK_PTS636Sx25SMTRLFS, F.Cu at (110.0, 115.0)
- added SW77: SW_Push, Button_Switch_SMD:SW_Tactile_SPST_NO_Straight_CK_PTS636Sx25SMTRLFS, F.Cu at (120.0, 115.0)
- added SW78: SW_Push, Button_Switch_SMD:SW_Tactile_SPST_NO_Straight_CK_PTS636Sx25SMTRLFS, F.Cu at (20.0, 130.0)
- added SW79: SW_Push, Button_Switch_SMD:SW_Tactile_SPST_NO_Straight_CK_PTS636Sx25SMTRLFS, F.Cu at (30.0, 130.0)
- added SW8: SW_Push, Button_Switch_SMD:SW_Tactile_SPST_NO_Straight_CK_PTS636Sx25SMTRLFS, F.Cu at (90.0, 25.0)
- added SW80: SW_Push, Button_Switch_SMD:SW_Tactile_SPST_NO_Straight_CK_PTS636Sx25SMTRLFS, F.Cu at (40.0, 130.0)
- added SW81: SW_Push, Button_Switch_SMD:SW_Tactile_SPST_NO_Straight_CK_PTS636Sx25SMTRLFS, F.Cu at (50.0, 130.0)
- added SW82: SW_Push, Button_Switch_SMD:SW_Tactile_SPST_NO_Straight_CK_PTS636Sx25SMTRLFS, F.Cu at (60.0, 130.0)
- added SW83: SW_Push, Button_Switch_SMD:SW_Tactile_SPST_NO_Straight_CK_PTS636Sx25SMTRLFS, F.Cu at (70.0, 130.0)
- added SW84: SW_Push, Button_Switch_SMD:SW_Tactile_SPST_NO_Straight_CK_PTS636Sx25SMTRLFS, F.Cu at (80.0, 130.0)
- added SW85: SW_Push, Button_Switch_SMD:SW_Tactile_SPST_NO_Straight_CK_PTS636Sx25SMTRLFS, F.Cu at (90.0, 130.0)
- added SW86: SW_Push, Button_Switch_SMD:SW_Tactile_SPST_NO_Straight_CK_PTS636Sx25SMTRLFS, F.Cu at (100.0, 130.0)
- added SW87: SW_Push, Button_Switch_SMD:SW_Tactile_SPST_NO_Straight_CK_PTS636Sx25SMTRLFS, F.Cu at (110.0, 130.0)
- added SW88: SW_Push, Button_Switch_SMD:SW_Tactile_SPST_NO_Straight_CK_PTS636Sx25SMTRLFS, F.Cu at (120.0, 130.0)
- added SW89: SW_Push, Button_Switch_SMD:SW_Tactile_SPST_NO_Straight_CK_PTS636Sx25SMTRLFS, F.Cu at (20.0, 145.0)
- added SW9: SW_Push, Button_Switch_SMD:SW_Tactile_SPST_NO_Straight_CK_PTS636Sx25SMTRLFS, F.Cu at (100.0, 25.0)
- added SW90: SW_Push, Button_Switch_SMD:SW_Tactile_SPST_NO_Straight_CK_PTS636Sx25SMTRLFS, F.Cu at (30.0, 145.0)
- added SW91: SW_Push, Button_Switch_SMD:SW_Tactile_SPST_NO_Straight_CK_PTS636Sx25SMTRLFS, F.Cu at (40.0, 145.0)
- added SW92: SW_Push, Button_Switch_SMD:SW_Tactile_SPST_NO_Straight_CK_PTS636Sx25SMTRLFS, F.Cu at (50.0, 145.0)
- added SW93: SW_Push, Button_Switch_SMD:SW_Tactile_SPST_NO_Straight_CK_PTS636Sx25SMTRLFS, F.Cu at (60.0, 145.0)
- added SW94: SW_Push, Button_Switch_SMD:SW_Tactile_SPST_NO_Straight_CK_PTS636Sx25SMTRLFS, F.Cu at (70.0, 145.0)
- added SW95: SW_Push, Button_Switch_SMD:SW_Tactile_SPST_NO_Straight_CK_PTS636Sx25SMTRLFS, F.Cu at (80.0, 145.0)
- added SW96: SW_Push, Button_Switch_SMD:SW_Tactile_SPST_NO_Straight_CK_PTS636Sx25SMTRLFS, F.Cu at (90.0, 145.0)
- added SW97: SW_Push, Button_Switch_SMD:SW_Tactile_SPST_NO_Straight_CK_PTS636Sx25SMTRLFS, F.Cu at (100.0, 145.0)
- added SW98: SW_Push, Button_Switch_SMD:SW_Tactile_SPST_NO_Straight_CK_PTS636Sx25SMTRLFS, F.Cu at (110.0, 145.0)
- added SW99: SW_Push, Button_Switch_SMD:SW_Tactile_SPST_NO_Straight_CK_PTS636Sx25SMTRLFS, F.Cu at (120.0, 145.0)
- U3: value ESP32_NODEMCU -> ESP32-DEVKIT-V1; footprint ESP32_NODEMCU:MODULE_ESP32_NODEMCU -> ESP32-DEVKIT-V1:MODULE_ESP32_DEVKIT_V1
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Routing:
- net Col2: track 0.00 -> 220.2 mm, vias 0 -> 14
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
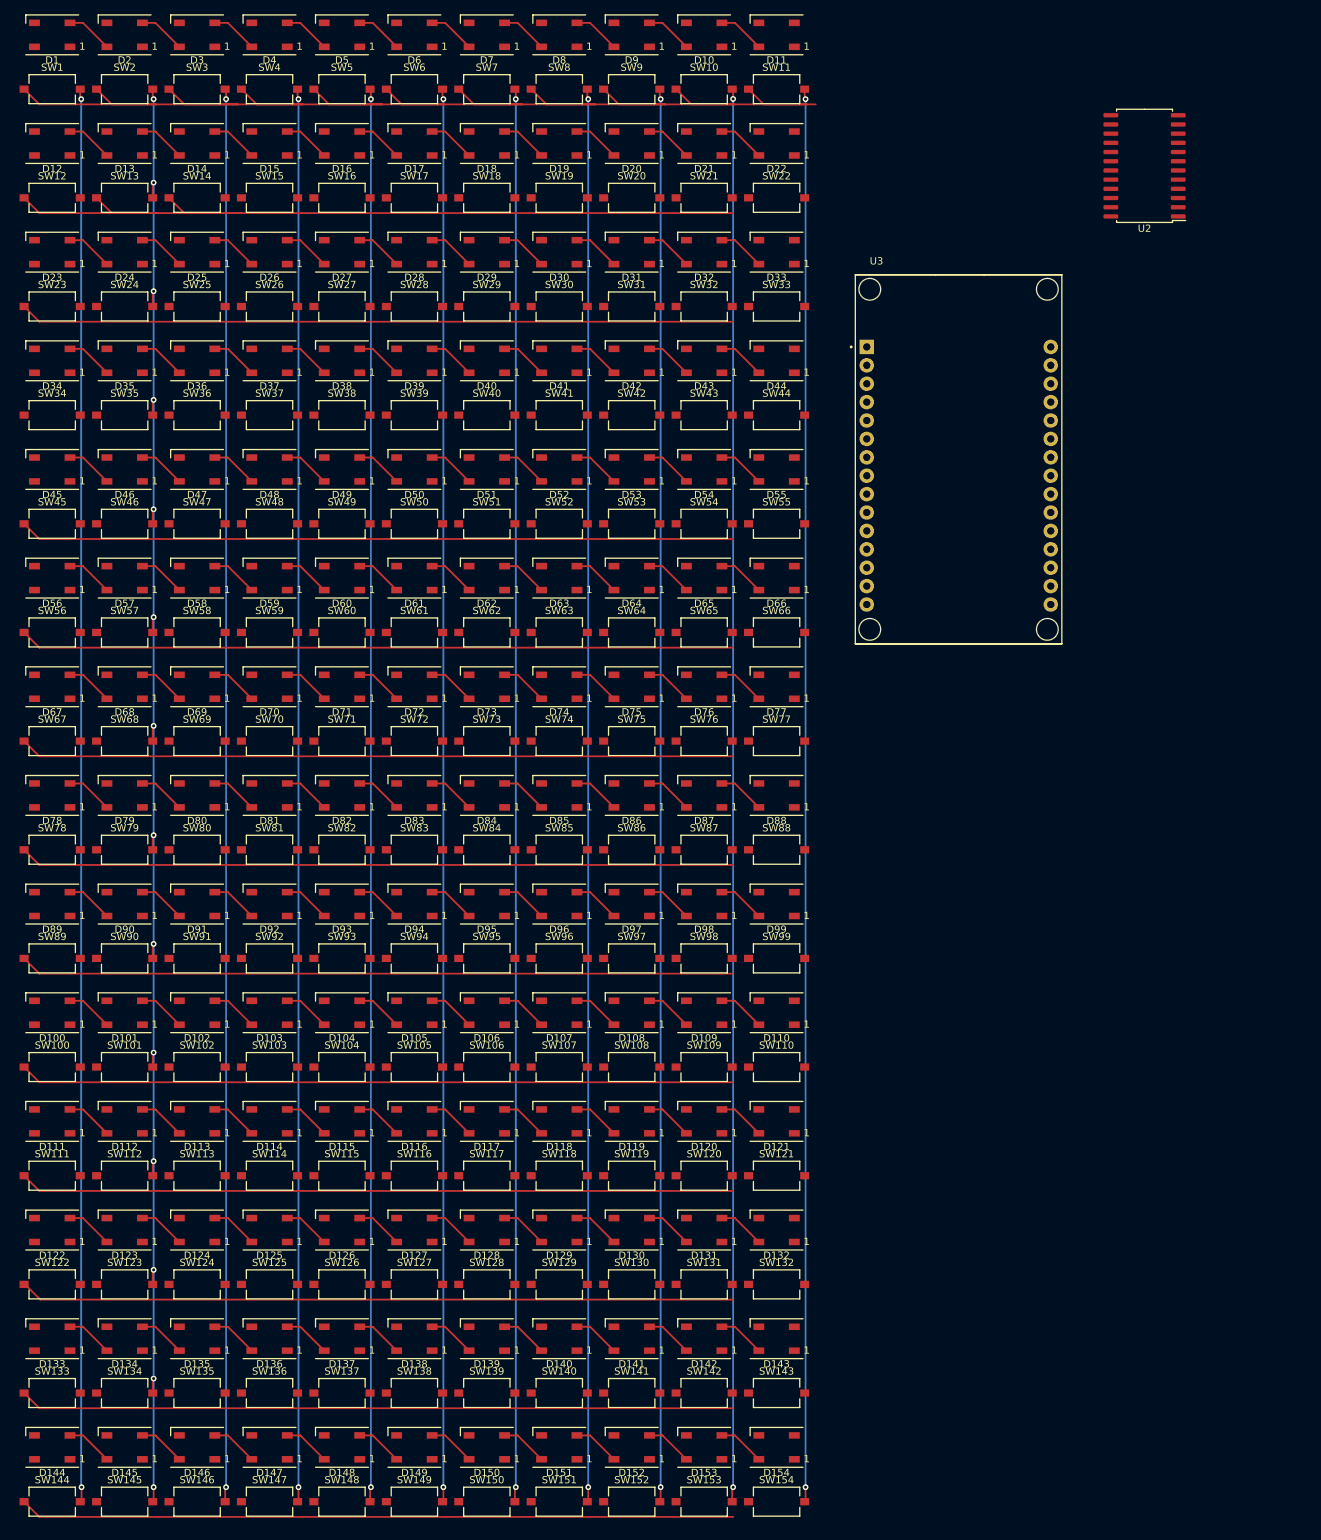
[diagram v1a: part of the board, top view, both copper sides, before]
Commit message: feat(pcb): route gnd
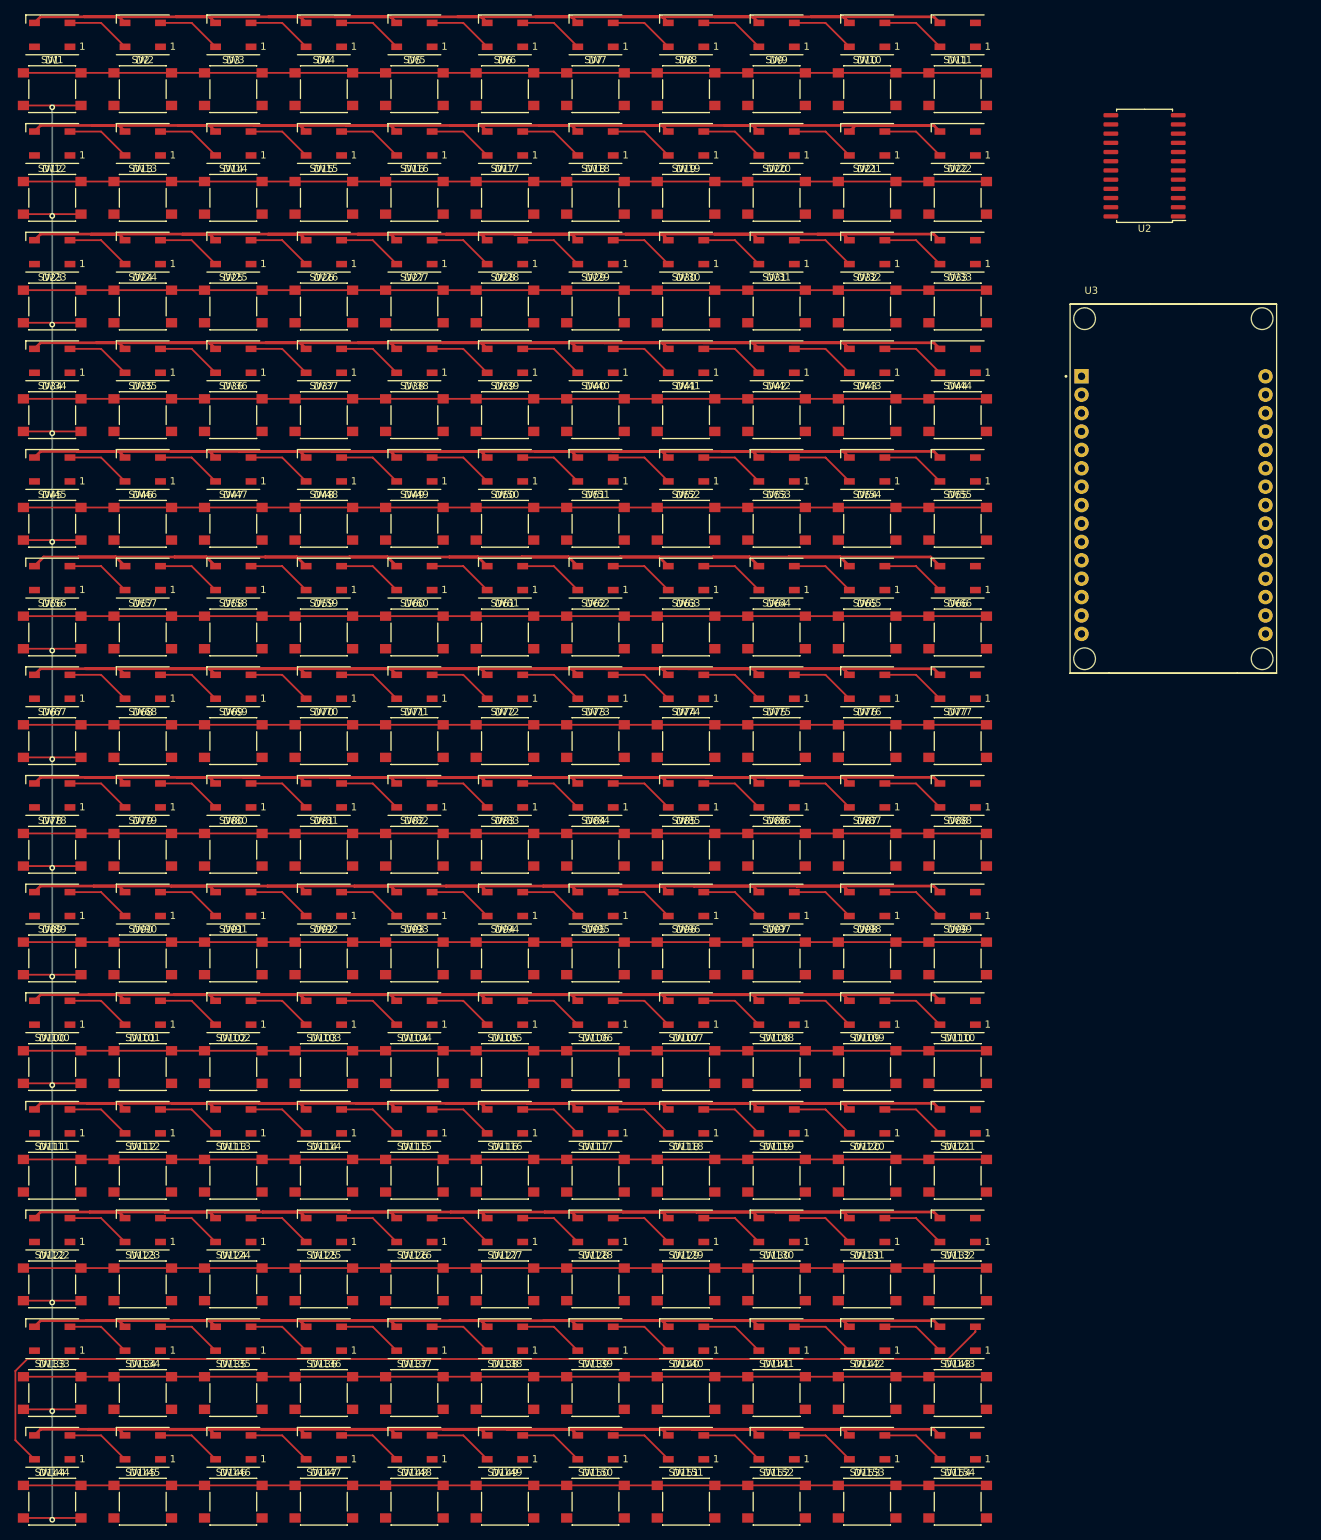
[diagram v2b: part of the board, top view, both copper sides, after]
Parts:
- SW1, SW10, SW100, SW101, SW102, SW103, SW104, SW105, SW106, SW107, SW108, SW109, SW11, SW110, SW111, SW112, SW113, SW114, SW115, SW116, SW117, SW118, SW119, SW12, SW120, SW121, SW122, SW123, SW124, SW125, SW126, SW127, SW128, SW129, SW13, SW130, SW131, SW132, SW133, SW134, SW135, SW136, SW137, SW138, SW139, SW14, SW140, SW141, SW142, SW143, SW144, SW145, SW146, SW147, SW148, SW149, SW15, SW150, SW151, SW152, SW153, SW154, SW16, SW17, SW18, SW19, SW2, SW20, SW21, SW22, SW23, SW24, SW25, SW26, SW27, SW28, SW29, SW3, SW30, SW31, SW32, SW33, SW34, SW35, SW36, SW37, SW38, SW39, SW4, SW40, SW41, SW42, SW43, SW44, SW45, SW46, SW47, SW48, SW49, SW5, SW50, SW51, SW52, SW53, SW54, SW55, SW56, SW57, SW58, SW59, SW6, SW60, SW61, SW62, SW63, SW64, SW65, SW66, SW67, SW68, SW69, SW7, SW70, SW71, SW72, SW73, SW74, SW75, SW76, SW77, SW78, SW79, SW8, SW80, SW81, SW82, SW83, SW84, SW85, SW86, SW87, SW88, SW89, SW9, SW90, SW91, SW92, SW93, SW94, SW95, SW96, SW97, SW98, SW99: footprint Button_Switch_SMD:SW_Tactile_SPST_NO_Straight_CK_PTS636Sx25SMTRLFS -> Button_Switch_SMD:SW_Push_1P1T_NO_6x6mm_H9.5mm
- moved U3 29.9 mm to (174.8, 80.2)
- moved D11 25.0 mm to (145.0, 17.5)
- moved D110 25.0 mm to (145.0, 152.5)
- moved D121 25.0 mm to (145.0, 167.5)
- moved D132 25.0 mm to (145.0, 182.5)
- moved D143 25.0 mm to (145.0, 197.5)
- moved D154 25.0 mm to (145.0, 212.5)
- moved D22 25.0 mm to (145.0, 32.5)
- moved D33 25.0 mm to (145.0, 47.5)
- moved D44 25.0 mm to (145.0, 62.5)
- moved D55 25.0 mm to (145.0, 77.5)
- moved D66 25.0 mm to (145.0, 92.5)
- moved D77 25.0 mm to (145.0, 107.5)
- moved D88 25.0 mm to (145.0, 122.5)
- moved D99 25.0 mm to (145.0, 137.5)
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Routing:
- net GND: track 0.00 -> 2645.7 mm
- net Col2: track 220.2 -> 0.00 mm, vias 14 -> 0
- net Col9: track 195.1 -> 0.00 mm, vias 2 -> 0
- net Col8: track 195.1 -> 0.00 mm, vias 2 -> 0
- net Col7: track 195.1 -> 0.00 mm, vias 2 -> 0
- net Col6: track 195.1 -> 0.00 mm, vias 2 -> 0
- net Col5: track 195.1 -> 0.00 mm, vias 2 -> 0
- net Col4: track 195.1 -> 0.00 mm, vias 2 -> 0
- net Col3: track 195.1 -> 0.00 mm, vias 2 -> 0
- net Col11: track 195.1 -> 0.00 mm, vias 2 -> 0
- net Col10: track 195.1 -> 0.00 mm, vias 2 -> 0
- net Net-(D143-DOUT): track 0.00 -> 148.8 mm
- net Row15: track 0.00 -> 132.9 mm
- net Col1: track 195.1 -> 301.0 mm, vias 2 -> 13
- net Row18: track 204.3 -> 132.9 mm
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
